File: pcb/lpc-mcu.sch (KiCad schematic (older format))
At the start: 12 parts, among them CON1 ARM-SWD-HEADER, IC1 LPC11U14FBD48, P4 GPIO, P6 GPIO2, X1 CRYSTAL

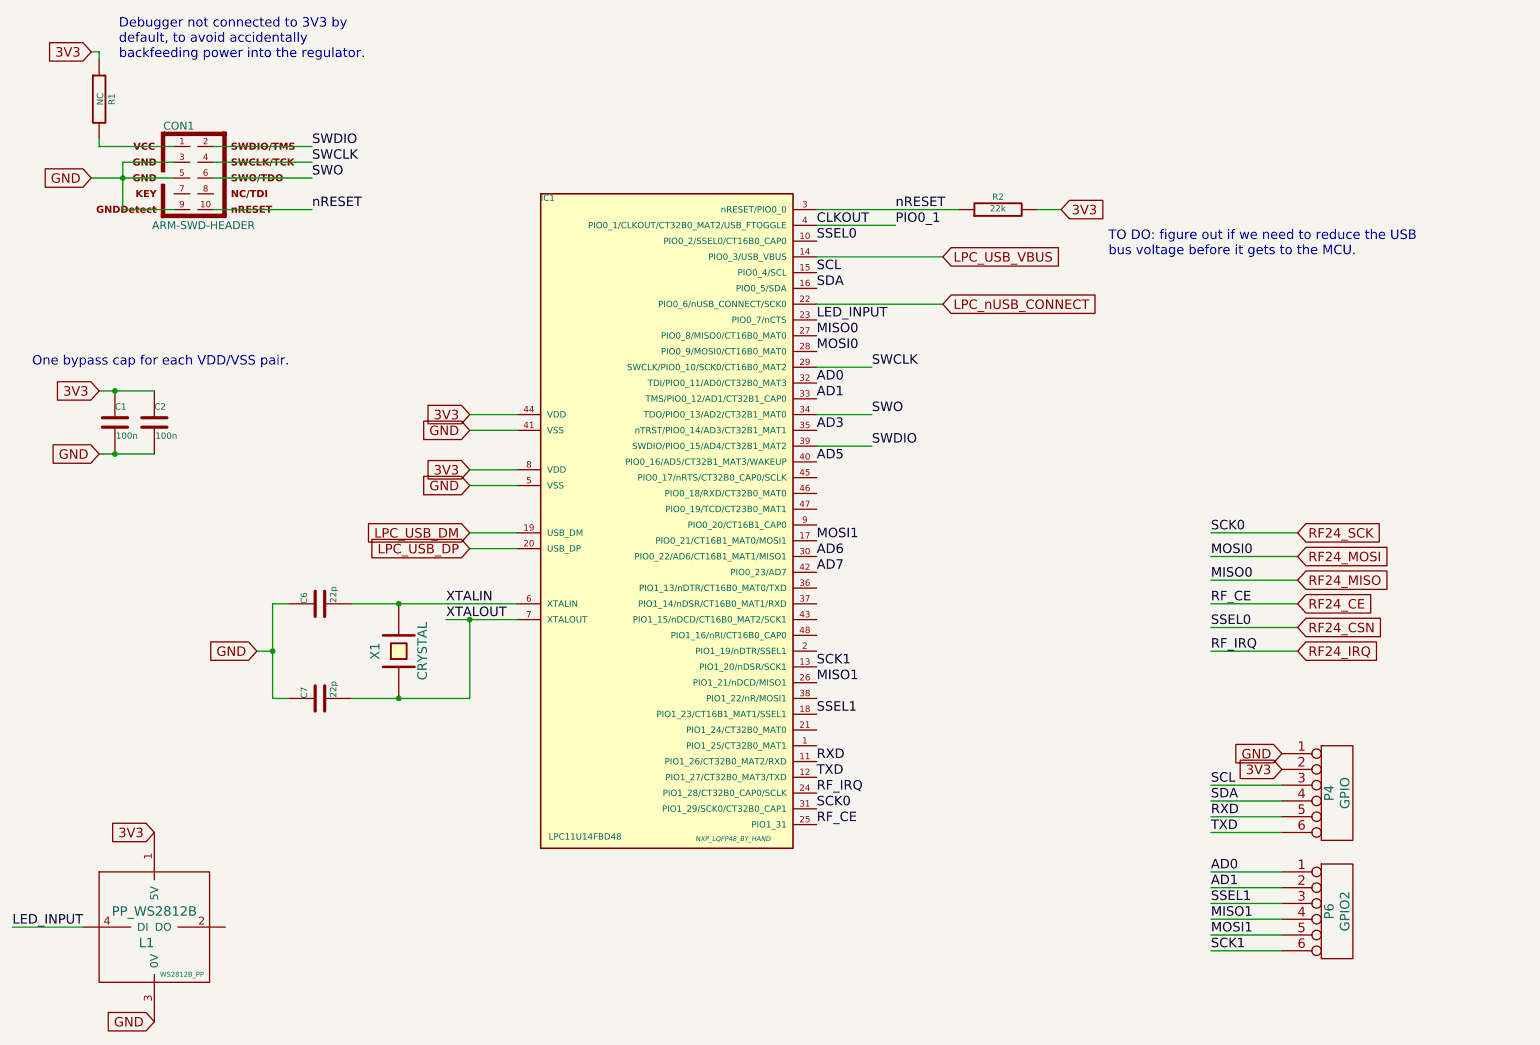
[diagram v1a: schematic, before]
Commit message: Upgraded all modules to new kicad_mod/pretty format.  Added MCP1700T-3302 regulator and cleaned up power circuit.  Getting closer to final power/USB placement.
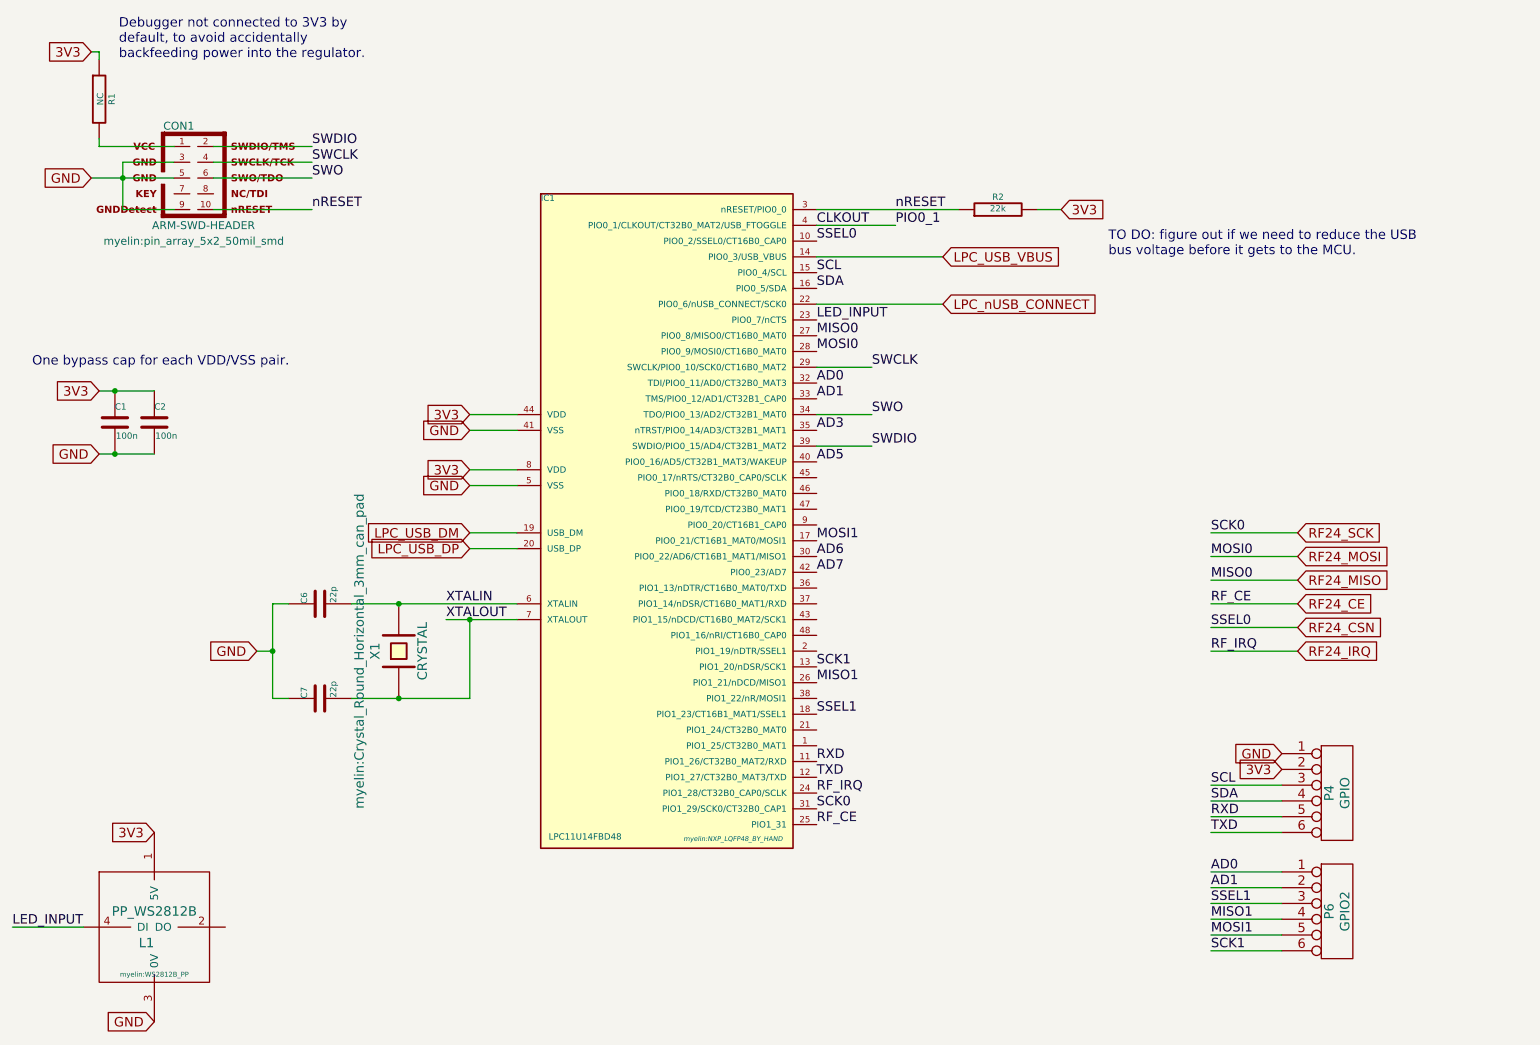
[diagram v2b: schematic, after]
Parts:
- CON1: footprint pin_array_5x2_50mil_smd -> myelin:pin_array_5x2_50mil_smd
- IC1: footprint NXP_LQFP48_BY_HAND -> myelin:NXP_LQFP48_BY_HAND
- L1: footprint WS2812B_PP -> myelin:WS2812B_PP
- X1: footprint ~ -> myelin:Crystal_Round_Horizontal_3mm_can_pad
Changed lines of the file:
@@
 LIBS:nRF24L01+
 LIBS:pp_ws2812b
+LIBS:mcp1700t-3302e-tt
 LIBS:modular-arm-usb-cache
 EELAYER 25 0
@@
 F 0 "IC1" H 4500 6250 40  0000 L BNN
 F 1 "LPC11U14FBD48" H 4550 2200 40  0000 L BNN
-F 2 "NXP_LQFP48_BY_HAND" H 5720 2210 30  0000 C CIN
+F 2 "myelin:NXP_LQFP48_BY_HAND" H 5720 2210 30  0000 C CIN
 F 3 "~" H 5250 4200 60  0000 C CNN
 	1    5250 4200
@@
 F 0 "CON1" H 2205 2330 50  0000 C CNN
 F 1 "ARM-SWD-HEADER" H 2035 1670 50  0000 L BNN
-F 2 "pin_array_5x2_50mil_smd" V 1875 2000 50  0001 C CNN
+F 2 "myelin:pin_array_5x2_50mil_smd" H 2300 1600 50  0000 C CNN
 F 3 "~" H 2375 2000 60  0000 C CNN
 	1    2300 2000
@@
 F 0 "X1" H 3600 5150 60  0000 C CNN
 F 1 "CRYSTAL" H 3600 4850 60  0000 C CNN
-F 2 "~" H 3600 5000 60  0000 C CNN
+F 2 "myelin:Crystal_Round_Horizontal_3mm_can_pad" H 3600 5250 60  0000 C CNN
 F 3 "~" H 3600 5000 60  0000 C CNN
 	1    3600 5000
@@
 F 0 "L1" H 2000 7350 60  0000 C CNN
 F 1 "PP_WS2812B" H 2050 7550 60  0000 C CNN
-F 2 "WS2812B_PP" H 2225 7150 31  0000 C CNN
+F 2 "myelin:WS2812B_PP" H 2050 7150 31  0000 C CNN
 F 3 "~" H 2050 7100 60  0000 C CNN
 	1    2050 7100

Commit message: moved things around on the pcb a bit, made it more compact
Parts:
- CON1: footprint myelin:pin_array_5x2_50mil_smd -> myelin:pin_array_5x2_50mil
- R1: footprint ~ -> Pin_Headers:Pin_Header_Straight_1x02
- X1: value CRYSTAL -> 16M xtal; symbol CRYSTAL -> CRYSTAL_SMD
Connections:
- net GND: now also X1.3 (case)
- net XTALIN: now also X1.1; no longer X1.2
- net XTALOUT: now also X1.2; no longer X1.1
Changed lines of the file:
@@
 F 0 "CON1" H 2205 2330 50  0000 C CNN
 F 1 "ARM-SWD-HEADER" H 2035 1670 50  0000 L BNN
-F 2 "myelin:pin_array_5x2_50mil_smd" H 2300 1600 50  0000 C CNN
+F 2 "myelin:pin_array_5x2_50mil" H 2300 1600 50  0000 C CNN
 F 3 "~" H 2375 2000 60  0000 C CNN
 	1    2300 2000
@@
 F 0 "R1" V 1780 1500 40  0000 C CNN
 F 1 "NC" V 1707 1501 40  0000 C CNN
-F 2 "~" V 1630 1500 30  0000 C CNN
+F 2 "Pin_Headers:Pin_Header_Straight_1x02" V 1630 1500 30  0000 C CNN
 F 3 "~" H 1700 1500 30  0000 C CNN
 	1    1700 1500
@@
 TO DO: figure out if we need to reduce the USB\nbus voltage before it gets to the MCU.
 $Comp
-L CRYSTAL X1
+L CRYSTAL_SMD X1
 U 1 1 549E7192
 P 3600 5000
 F 0 "X1" H 3600 5150 60  0000 C CNN
-F 1 "CRYSTAL" H 3600 4850 60  0000 C CNN
+F 1 "16M xtal" H 3600 4850 60  0000 C CNN
 F 2 "myelin:Crystal_Round_Horizontal_3mm_can_pad" H 3600 5250 60  0000 C CNN
 F 3 "~" H 3600 5000 60  0000 C CNN
 	1    3600 5000
-	0    -1   -1   0
+	0    1    1    0
 $EndComp
 $Comp
@@
 	2800 5300 2900 5300
 Wire Wire Line
-	2700 5000 2800 5000
+	2700 5000 3500 5000
 Connection ~ 2800 5000
 Wire Wire Line
@@
 Text Label 8750 6600 0    60   ~ 0
 SSEL1
+Wire Wire Line
+	3600 4800 3600 4700
+Wire Wire Line
+	3600 5300 3600 5200
 $EndSCHEMATC
